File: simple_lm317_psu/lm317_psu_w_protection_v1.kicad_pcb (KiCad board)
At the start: 2 copper layers, 50 x 32.9 mm, 12 parts, among them J1 Bornera, U1 LM317

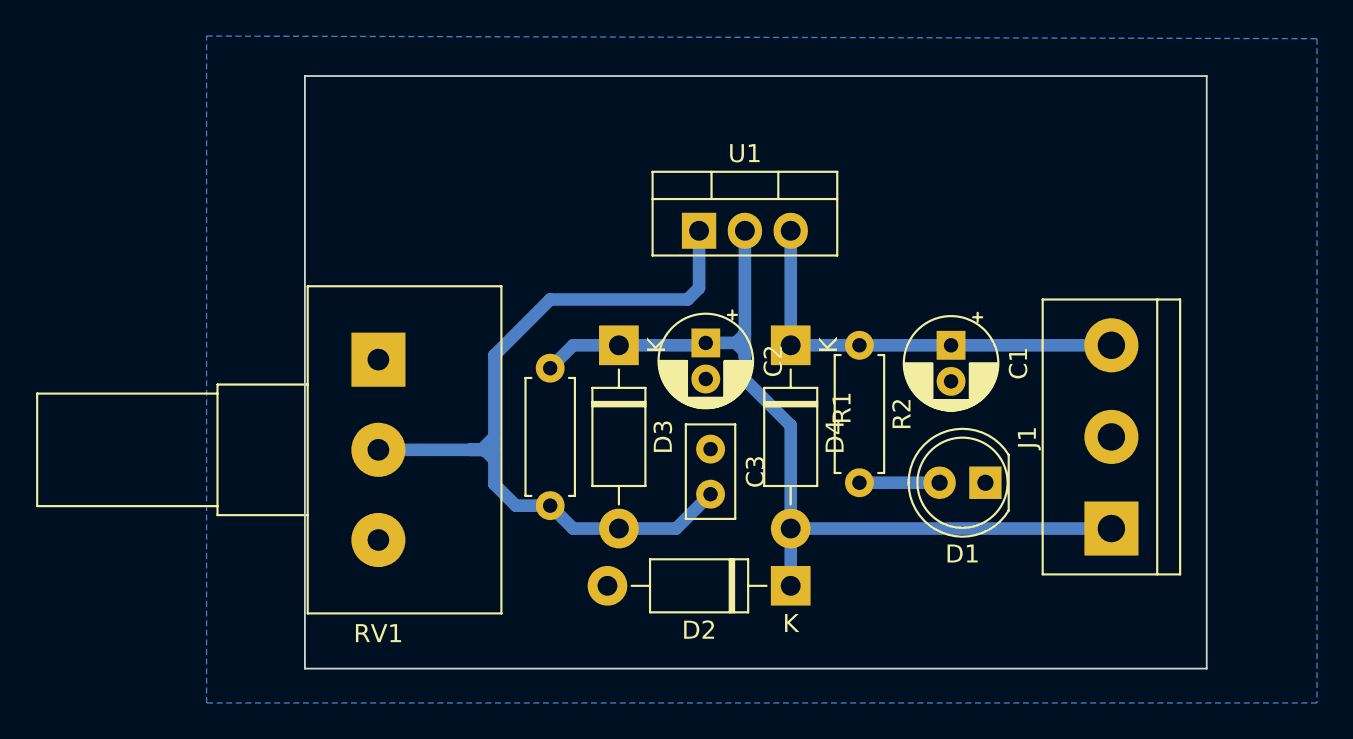
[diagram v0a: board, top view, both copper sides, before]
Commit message: Simple PSU LM317 based
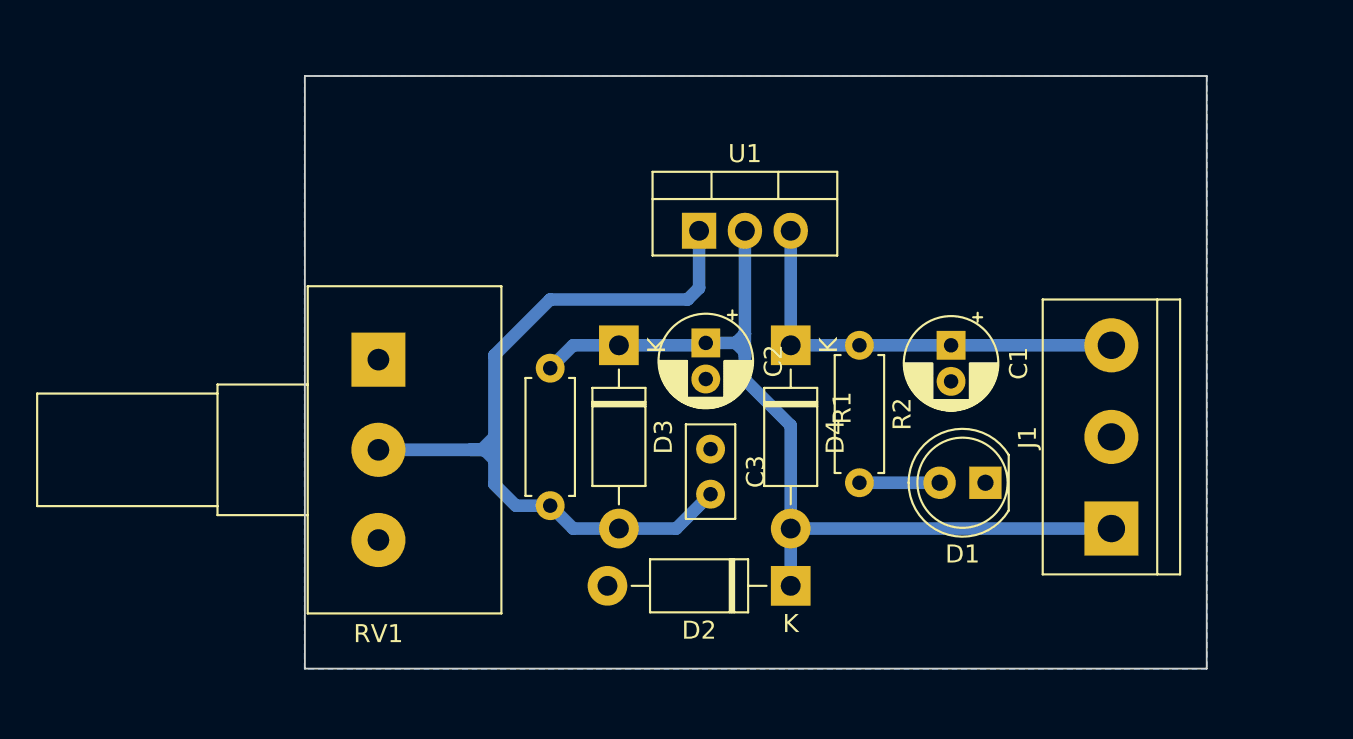
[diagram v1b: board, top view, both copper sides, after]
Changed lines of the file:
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@@
     )
   )
-  (gr_line (start 117.505 77.325) (end 170.21 77.325)
+  (gr_line (start 117.856 77.2) (end 167.85 77.216)
     (stroke (width 0.15) (type default)) (layer "Dwgs.User"))
   (gr_rect (start 117.875 71.92) (end 167.875 104.775)
@@
     (polygon
       (pts
-        (xy 112.425 69.705)
-        (xy 173.99 69.85)
-        (xy 173.99 106.68)
-        (xy 112.425 106.68)
+        (xy 117.85 71.9)
+        (xy 167.9 71.9)
+        (xy 167.9 104.8)
+        (xy 117.85 104.8)
       )
     )

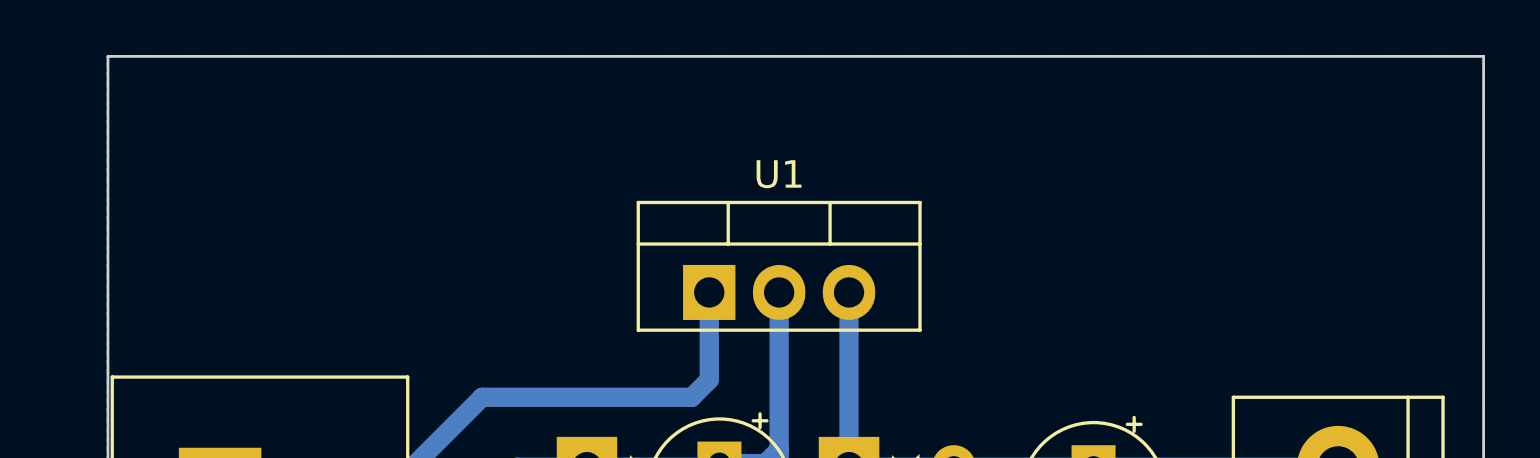
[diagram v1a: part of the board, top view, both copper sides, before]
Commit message: [ADD] LM317 CV PSU (with minimal protecctions)
WIP - Add CC protections
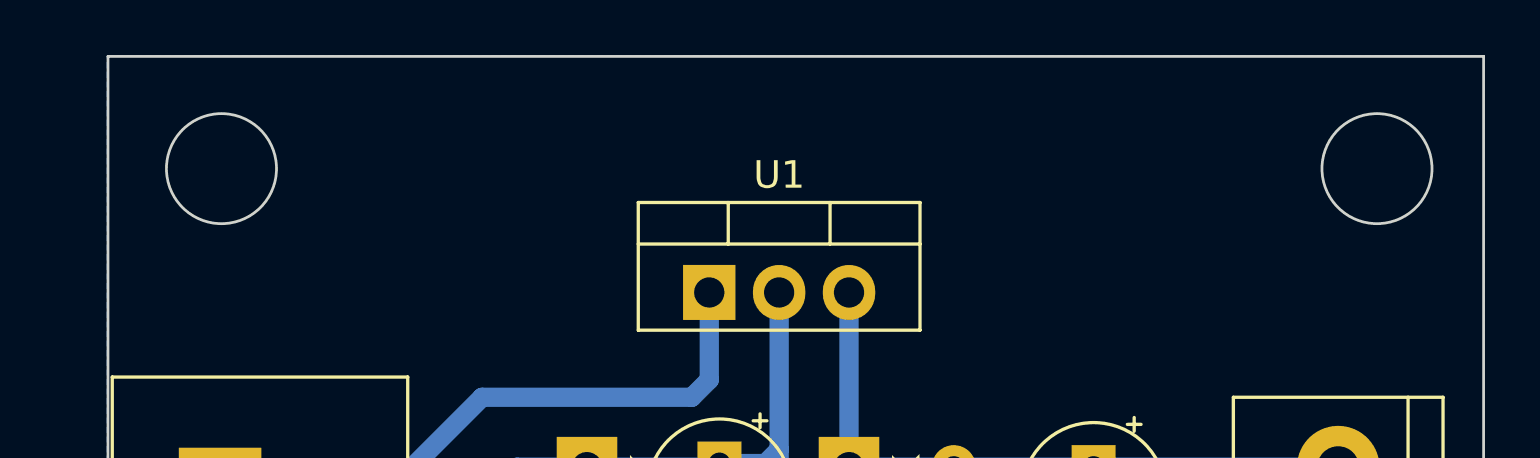
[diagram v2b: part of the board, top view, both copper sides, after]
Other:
- outline, holes or cut-outs redrawn
